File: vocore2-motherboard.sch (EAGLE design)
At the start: 92 parts, among them IC1 AP63205, IC2 FE1.1S, IC3 LM3761MF-3.3, IC4 LM3761MF-3.3, IC5 LM3761MF-3.3, IC6 FT232R, IC7 742G17DBV, J1 RJHSE-5381, J2 TE_1775470-8, J3 AMPHENOL_1140084168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

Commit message: fix: moved LAN_LED_ACT to gpio43
gpio43 can be configured to represent the LNK/ACT state of the Ethernt
PHYs Port 0.
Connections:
- removed net N$47: U1.GPIO43
- new net N$34: U1.GPIO37
- net LED_LAN_ACT: now also IC7B.I, U1.GPIO43; no longer IC7A.I, U1.GPIO37
- net LED_LAN_LNK: now also IC7A.I; no longer IC7B.I
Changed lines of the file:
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@@
 <wire x1="78.74" y1="142.24" x2="78.74" y2="144.78" width="0.1524" layer="91"/>
 <junction x="78.74" y="142.24"/>
+<junction x="40.64" y="142.24"/>
 </segment>
 <segment>
@@
 <net name="LED_LAN_ACT" class="0">
 <segment>
-<pinref part="U1" gate="G$1" pin="GPIO37"/>
-<wire x1="106.68" y1="73.66" x2="109.22" y2="73.66" width="0.1524" layer="91"/>
-<label x="109.22" y="73.66" size="1.27" layer="95" xref="yes"/>
+<pinref part="U1" gate="G$1" pin="GPIO43"/>
+<wire x1="106.68" y1="58.42" x2="111.76" y2="58.42" width="0.1524" layer="91"/>
+<label x="111.76" y="58.42" size="1.27" layer="95" xref="yes"/>
 </segment>
 </net>
@@
 <pinref part="U1" gate="G$1" pin="GPIO42"/>
 <wire x1="106.68" y1="60.96" x2="109.22" y2="60.96" width="0.1524" layer="91"/>
-</segment>
-</net>
-<net name="N$47" class="0">
-<segment>
-<pinref part="U1" gate="G$1" pin="GPIO43"/>
-<wire x1="106.68" y1="58.42" x2="109.22" y2="58.42" width="0.1524" layer="91"/>
 </segment>
 </net>
@@
 <pinref part="SP1" gate="G$1" pin="2"/>
 <wire x1="15.24" y1="25.4" x2="15.24" y2="27.94" width="0.1524" layer="91"/>
+</segment>
+</net>
+<net name="N$34" class="0">
+<segment>
+<pinref part="U1" gate="G$1" pin="GPIO37"/>
+<wire x1="106.68" y1="73.66" x2="109.22" y2="73.66" width="0.1524" layer="91"/>
 </segment>
 </net>
@@
 </segment>
 </net>
-<net name="LED_LAN_ACT" class="0">
+<net name="N$67" class="0">
+<segment>
+<pinref part="IC7" gate="B" pin="O"/>
+<pinref part="R14" gate="G$1" pin="1"/>
+<wire x1="238.76" y1="96.52" x2="215.9" y2="96.52" width="0.1524" layer="91"/>
+</segment>
+</net>
+<net name="LED_LAN_LNK" class="0">
 <segment>
 <pinref part="IC7" gate="A" pin="I"/>
@@
 </segment>
 </net>
-<net name="N$67" class="0">
-<segment>
-<pinref part="IC7" gate="B" pin="O"/>
-<pinref part="R14" gate="G$1" pin="1"/>
-<wire x1="238.76" y1="96.52" x2="215.9" y2="96.52" width="0.1524" layer="91"/>
-</segment>
-</net>
-<net name="LED_LAN_LNK" class="0">
+<net name="VC_3V3" class="0">
+<segment>
+<pinref part="IC7" gate="C" pin="VCC"/>
+<wire x1="233.68" y1="144.78" x2="233.68" y2="147.32" width="0.1524" layer="91"/>
+<label x="233.68" y="147.32" size="1.27" layer="95" rot="R90" xref="yes"/>
+</segment>
+</net>
+<net name="LED_LAN_ACT" class="0">
 <segment>
 <pinref part="IC7" gate="B" pin="I"/>
@@
 </segment>
 </net>
-<net name="VC_3V3" class="0">
-<segment>
-<pinref part="IC7" gate="C" pin="VCC"/>
-<wire x1="233.68" y1="144.78" x2="233.68" y2="147.32" width="0.1524" layer="91"/>
-<label x="233.68" y="147.32" size="1.27" layer="95" rot="R90" xref="yes"/>
-</segment>
-</net>

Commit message: fix: typo in partname LM3761MF -> LM3671MF
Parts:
- IC3, IC4, IC5: value LM3761MF-3.3 -> LM3671MF-3.3
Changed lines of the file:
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@@
 <part name="GND9" library="supply1" deviceset="GND" device=""/>
 <part name="R3" library="rcl" library_urn="urn:adsk.eagle:library:334" deviceset="R-EU_" device="R0603" package3d_urn="urn:adsk.eagle:package:23555/3" value="330R"/>
-<part name="IC4" library="texas" deviceset="LM3671" device="" value="LM3761MF-3.3">
+<part name="IC4" library="texas" deviceset="LM3671" device="" value="LM3671MF-3.3">
 <attribute name="FARNELL" value="1685767"/>
 <attribute name="MBM" value="1"/>
@@
 <part name="GND65" library="supply1" deviceset="GND" device=""/>
 <part name="FRAME4" library="frames" library_urn="urn:adsk.eagle:library:229" deviceset="A4L-LOC" device=""/>
-<part name="IC3" library="texas" deviceset="LM3671" device="" value="LM3761MF-3.3">
+<part name="IC3" library="texas" deviceset="LM3671" device="" value="LM3671MF-3.3">
 <attribute name="FARNELL" value="1685767"/>
 <attribute name="MBM" value="1"/>
@@
 </part>
 <part name="GND14" library="supply1" deviceset="GND" device=""/>
-<part name="IC5" library="texas" deviceset="LM3671" device="" value="LM3761MF-3.3">
+<part name="IC5" library="texas" deviceset="LM3671" device="" value="LM3671MF-3.3">
 <attribute name="FARNELL" value="1685767"/>
 <attribute name="MBM" value="1"/>

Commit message: feat: added digikey part numbers
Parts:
- C11, C13, C32: BUERKLIN 53D2086 -> (none); DIGIKEY (none) -> 1276-2087-1-ND; MBM 10 -> (none); PREIS 0,10 -> (none)
- C20, C21, C22, C23: DIGIKEY (none) -> 490-4780-1-ND
- C24: DIGIKEY (none) -> 399-7246-1-ND
- D4: DIGIKEY (none) -> 1727-3884-1-ND; MBM 5 -> (none); PREIS 0,311 -> (none)
- IC3, IC4, IC5: DIGIKEY (none) -> LM3671MF-3.3/NOPBCT-ND; MBM 1 -> (none); PREIS 0,704 -> (none)
- IC7: DIGIKEY (none) -> 296-SN74LVC2G17DBVRCT-ND; MBM 1 -> (none); PREIS 0,616 -> (none)
- L10, L2, L3: DIGIKEY (none) -> 445-8725-1-ND; MBM 1 -> (none); PREIS 1,70 -> (none)
- L8: DIGIKEY (none) -> 490-1054-1-ND; FARNELL 1515661 -> (none); MBM 10 -> (none); PREIS 0,0595 -> (none)
- Q1: DIGIKEY (none) -> BSS123LT1GOSCT-ND‎
- R1: DIGIKEY (none) -> RR08P2.7KDCT-ND
- R12, R13, R8, R9: value (none) -> 75R; DIGIKEY (none) -> RNCP0603FTD75R0CT-ND‎

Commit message: fix: proper colors for leds
PWR = red
MPCIE_PWR = orange
MPCIE_USB = green
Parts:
- LED1, LED2, LED4: value GREEN -> ORANGE
- LED3: value GREEN -> RED
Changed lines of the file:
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@@
 <attribute name="SPICEPREFIX" value="G"/>
 </part>
-<part name="LED3" library="led" library_urn="urn:adsk.eagle:library:259" deviceset="LED" device="CHIP-LED0805" package3d_urn="urn:adsk.eagle:package:15818/2" value="GREEN">
+<part name="LED3" library="led" library_urn="urn:adsk.eagle:library:259" deviceset="LED" device="CHIP-LED0805" package3d_urn="urn:adsk.eagle:package:15818/2" value="RED">
 <attribute name="FARNELL" value="1686076"/>
 <attribute name="MBM" value="5"/>
@@
 </part>
 <part name="GND17" library="supply1" deviceset="GND" device=""/>
-<part name="LED1" library="led" library_urn="urn:adsk.eagle:library:259" deviceset="LED" device="CHIP-LED0805" package3d_urn="urn:adsk.eagle:package:15818/2" value="GREEN">
+<part name="LED1" library="led" library_urn="urn:adsk.eagle:library:259" deviceset="LED" device="CHIP-LED0805" package3d_urn="urn:adsk.eagle:package:15818/2" value="ORANGE">
 <attribute name="FARNELL" value="1686076"/>
 <attribute name="MBM" value="5"/>
@@
 <part name="GND18" library="supply1" deviceset="GND" device=""/>
 <part name="R2" library="rcl" library_urn="urn:adsk.eagle:library:334" deviceset="R-EU_" device="R0603" package3d_urn="urn:adsk.eagle:package:23555/3" value="330R"/>
-<part name="LED2" library="led" library_urn="urn:adsk.eagle:library:259" deviceset="LED" device="CHIP-LED0805" package3d_urn="urn:adsk.eagle:package:15818/2" value="GREEN">
+<part name="LED2" library="led" library_urn="urn:adsk.eagle:library:259" deviceset="LED" device="CHIP-LED0805" package3d_urn="urn:adsk.eagle:package:15818/2" value="ORANGE">
 <attribute name="FARNELL" value="1686076"/>
 <attribute name="MBM" value="5"/>
@@
 <part name="GND19" library="supply1" deviceset="GND" device=""/>
 <part name="R4" library="rcl" library_urn="urn:adsk.eagle:library:334" deviceset="R-EU_" device="R0603" package3d_urn="urn:adsk.eagle:package:23555/3" value="330R"/>
-<part name="LED4" library="led" library_urn="urn:adsk.eagle:library:259" deviceset="LED" device="CHIP-LED0805" package3d_urn="urn:adsk.eagle:package:15818/2" value="GREEN">
+<part name="LED4" library="led" library_urn="urn:adsk.eagle:library:259" deviceset="LED" device="CHIP-LED0805" package3d_urn="urn:adsk.eagle:package:15818/2" value="ORANGE">
 <attribute name="FARNELL" value="1686076"/>
 <attribute name="MBM" value="5"/>

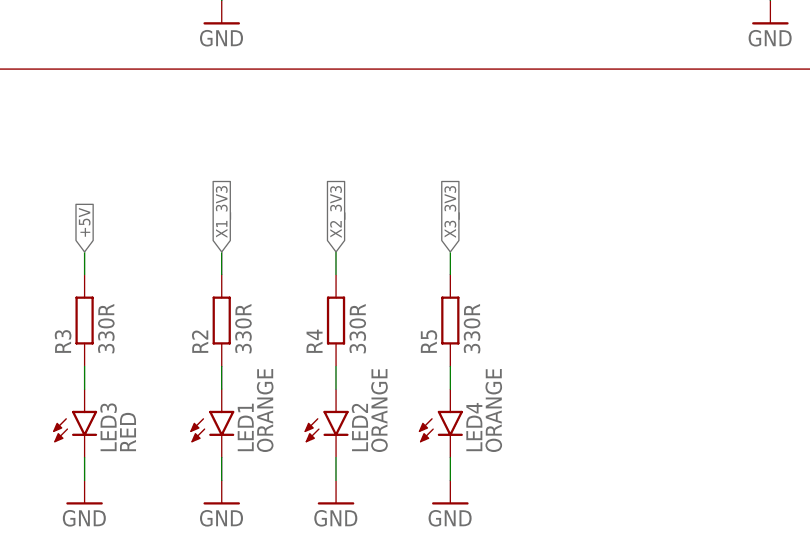
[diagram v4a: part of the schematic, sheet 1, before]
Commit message: fix: corrected led restistor values
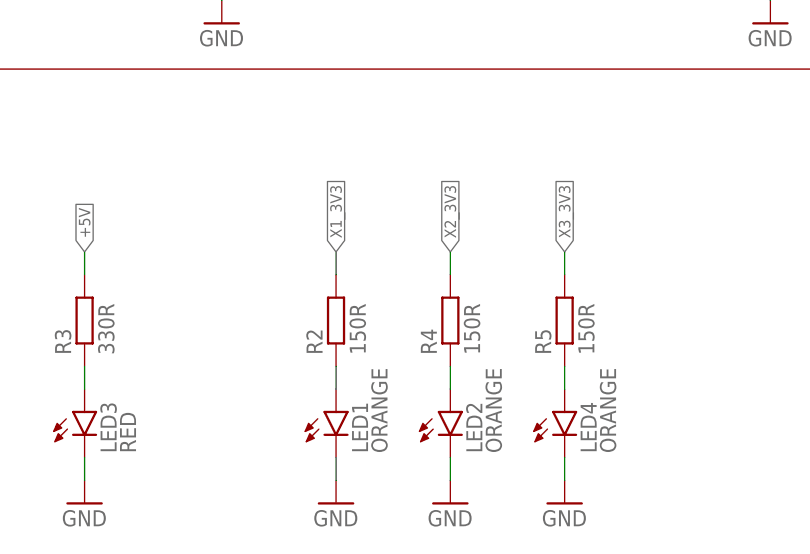
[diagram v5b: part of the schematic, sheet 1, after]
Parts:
- LED1, LED2, LED4: DIGIKEY (none) -> 160-1445-1-ND; FARNELL 1686076 -> (none); MBM 5 -> (none); PREIS 0,20 -> (none); SPICEPREFIX B -> (none)
- LED3: DIGIKEY (none) -> 160-1447-1-ND; FARNELL 1686076 -> (none); MBM 5 -> (none); PREIS 0,20 -> (none); SPICEPREFIX B -> (none)
- LED5, LED6, LED7: DIGIKEY (none) -> 160-1446-1-ND; FARNELL 1686076 -> (none); MBM 5 -> (none); PREIS 0,20 -> (none); SPICEPREFIX B -> (none)
- R10, R2, R4, R5, R6: value 330R -> 150R
- R14, R15: value 330R -> 820R; DIGIKEY (none) -> A129687CT-ND
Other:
- note added: "I=10mA @ Vf=2V"
- moved on the sheet: LED1, LED2, LED4, R2, R4, R5

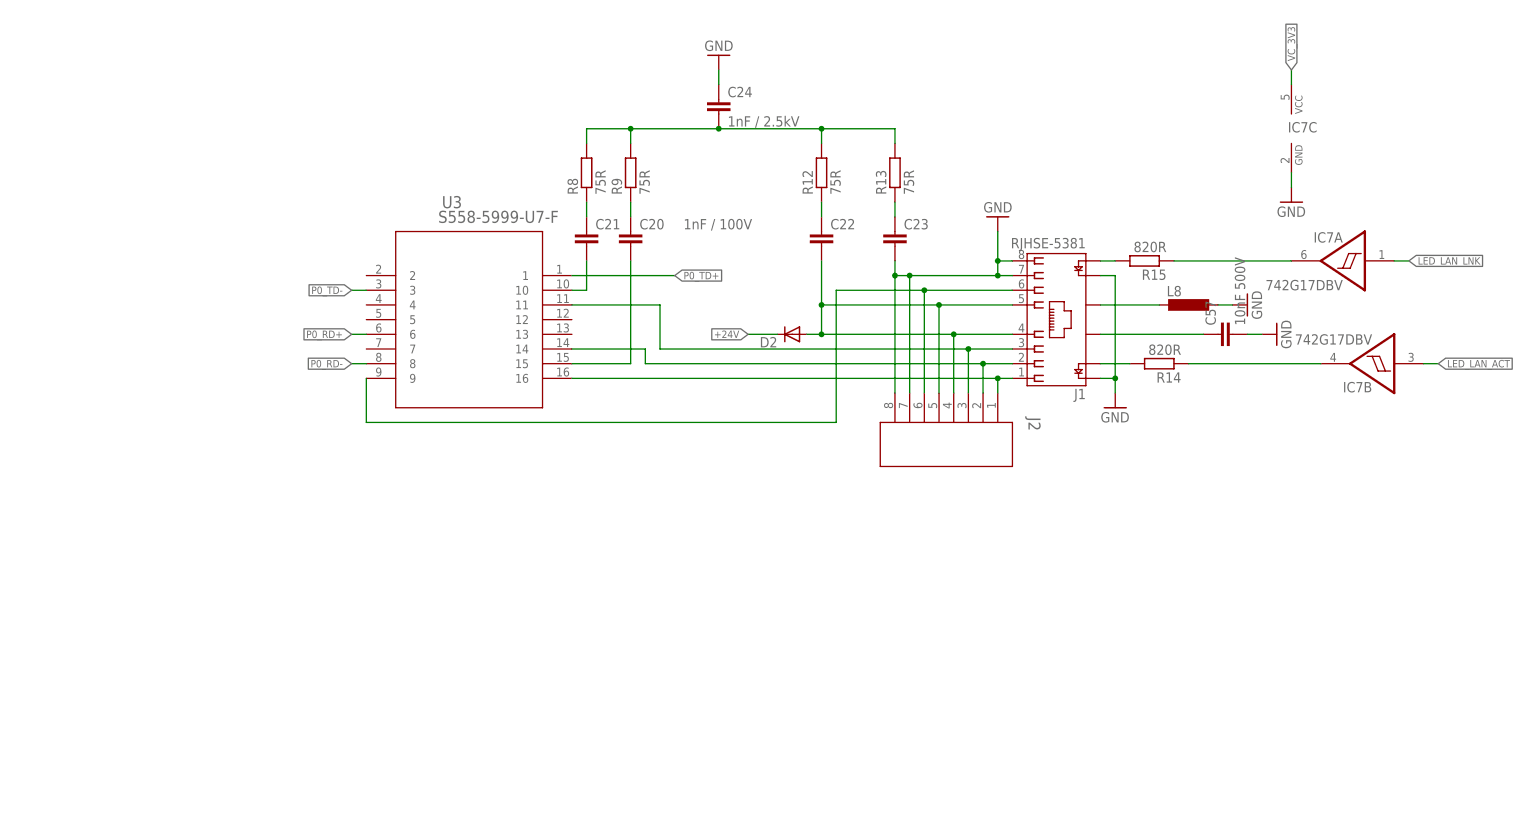
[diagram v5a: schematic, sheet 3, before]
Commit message: fix: some more digikey part numbers
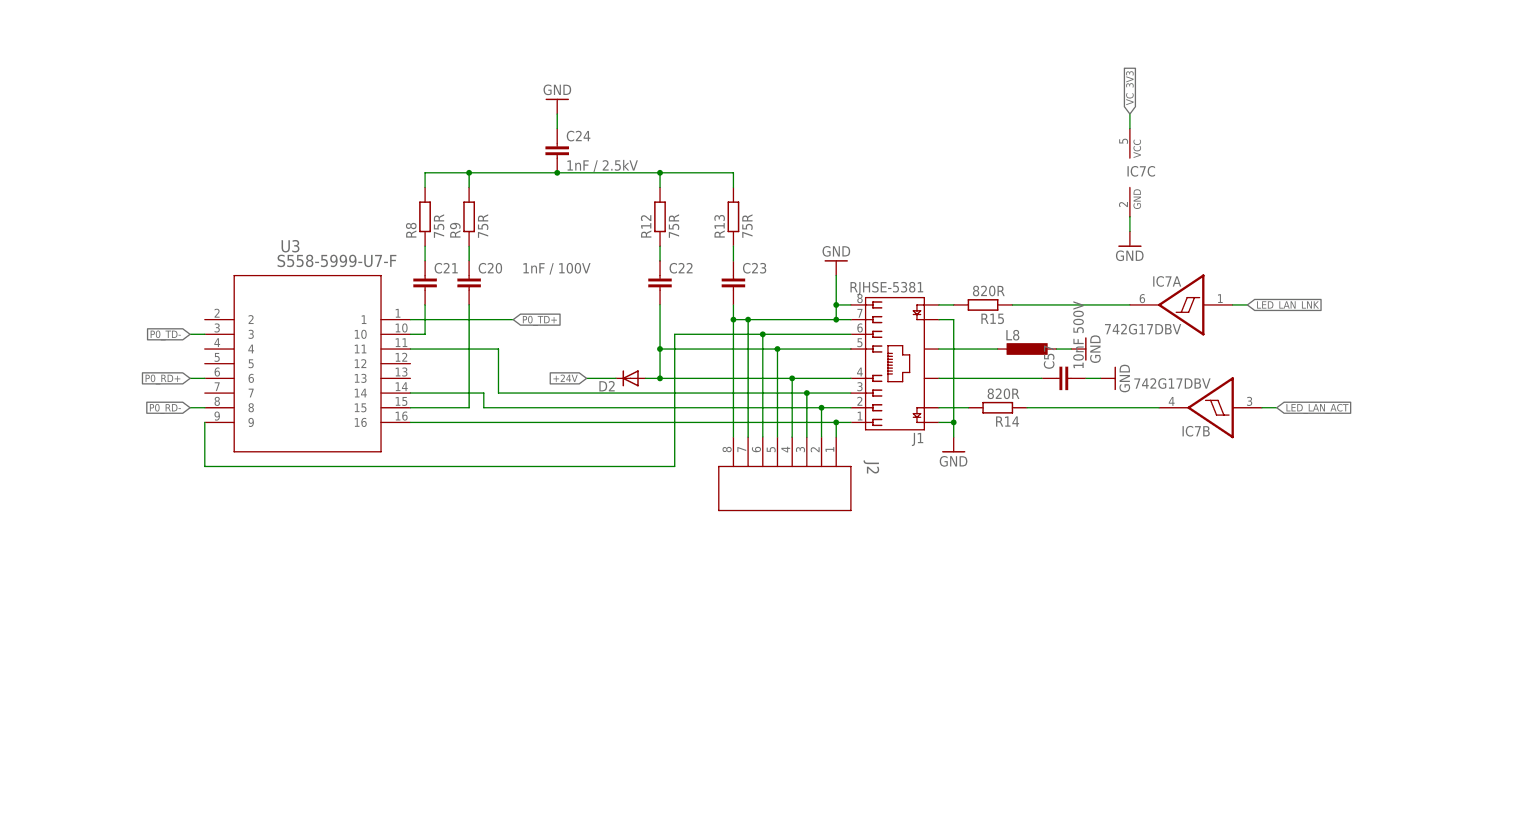
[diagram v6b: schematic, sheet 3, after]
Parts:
- X5: DIGIKEY (none) -> ‎277-1207-ND‎;‎277-13872-ND‎
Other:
- moved on the sheet: C20, C21, C22, C23, C24, C57, D2, IC7A, IC7B, IC7C, J1, J2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

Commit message: refactor: new symbol for ethernet transformer U4
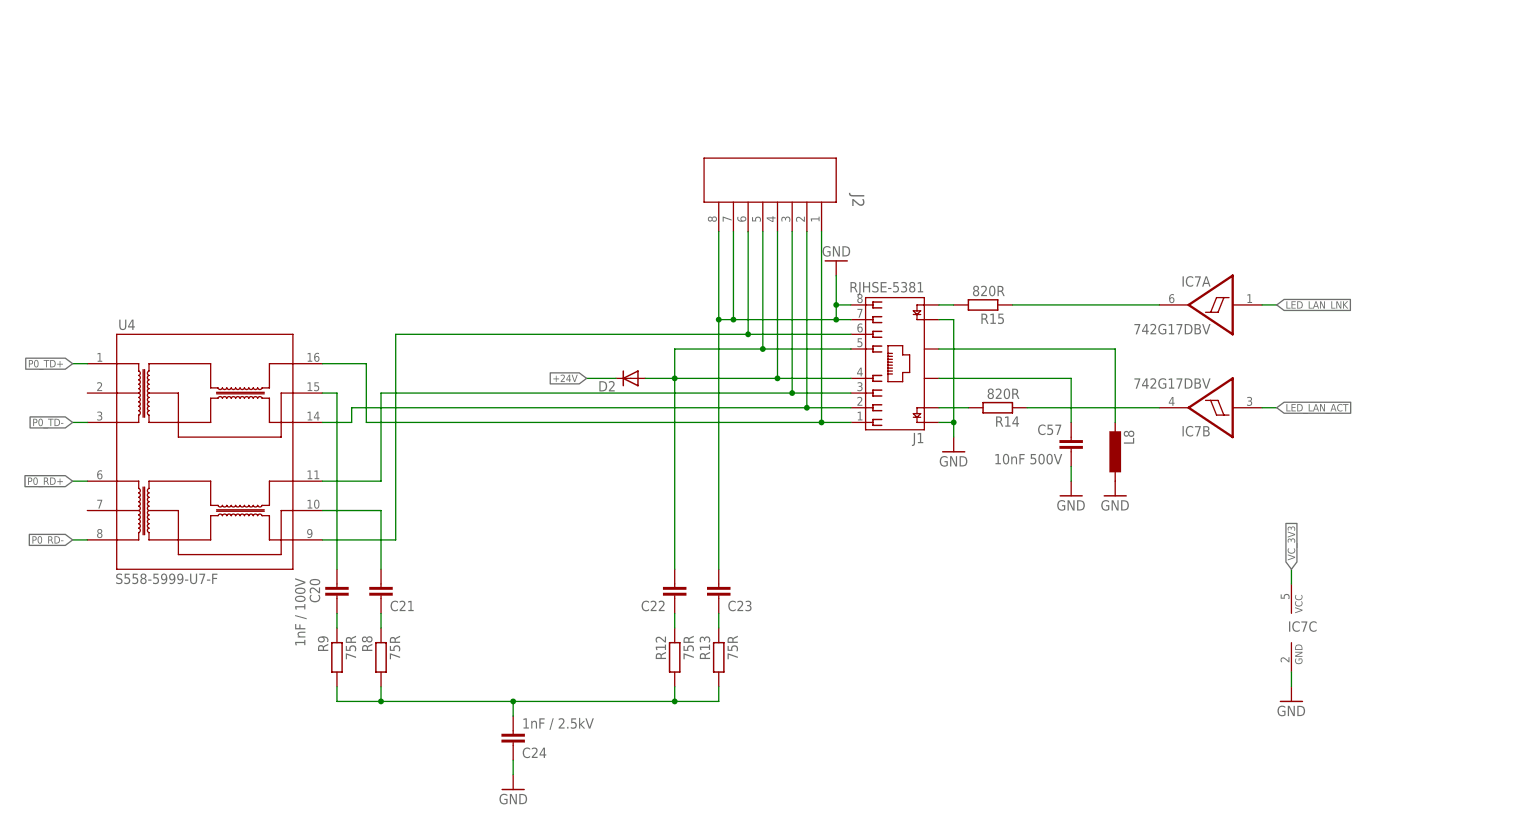
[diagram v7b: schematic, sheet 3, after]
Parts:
- removed U3: S558-5999-U7-F, ethernet-transformer:S558-5999-U7-F
- added U4: S558-5999-U7-F, ethernet-transformer:S558-5999-U7-F
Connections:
- net N$16: now also U4.RX_CT; no longer U3.10
- net N$7: now also U4.TX_CT; no longer U3.15
- net P0_RD+: now also U4.RD+; no longer U3.6
- net P0_RD-: now also U4.RD-; no longer U3.8
- net P0_TD+: now also U4.TD+; no longer U3.1
- net P0_TD-: now also U4.TD-; no longer U3.3
- net RX+: now also U4.RX+; no longer U3.11
- net RX-: now also U4.RX-; no longer U3.9
- net TX+: now also U4.TX+; no longer U3.16
- net TX-: now also U4.TX-; no longer U3.14
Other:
- moved on the sheet: C20, C21, C22, C23, C24, C57, IC7A, IC7C, J2, L8, R12, R13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

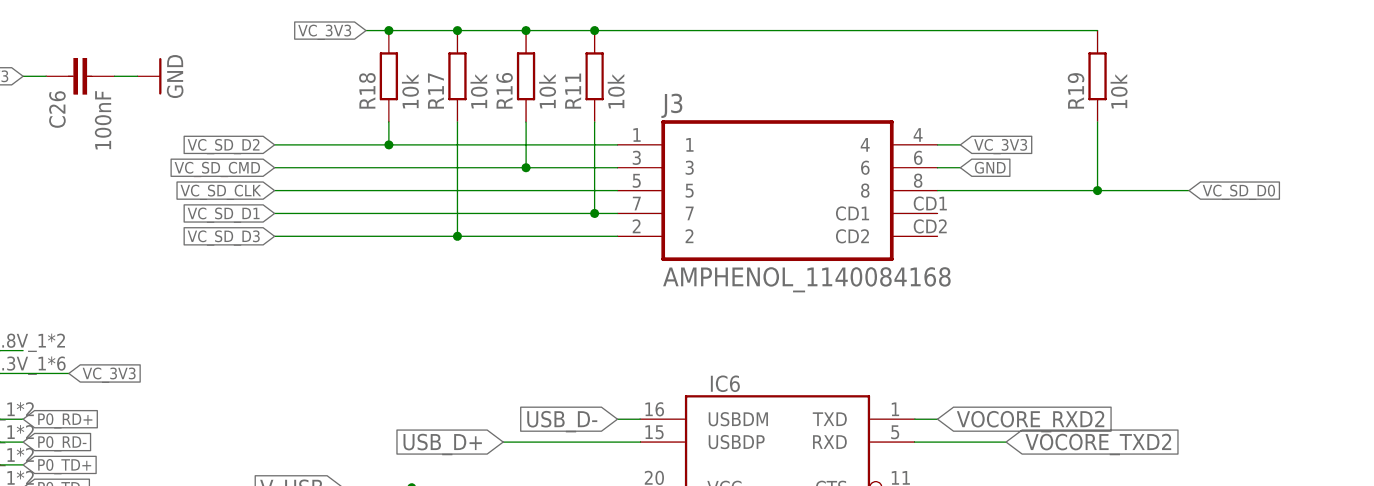
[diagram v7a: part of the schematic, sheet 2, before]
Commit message: fix: switched SD_D0 and SD_D1
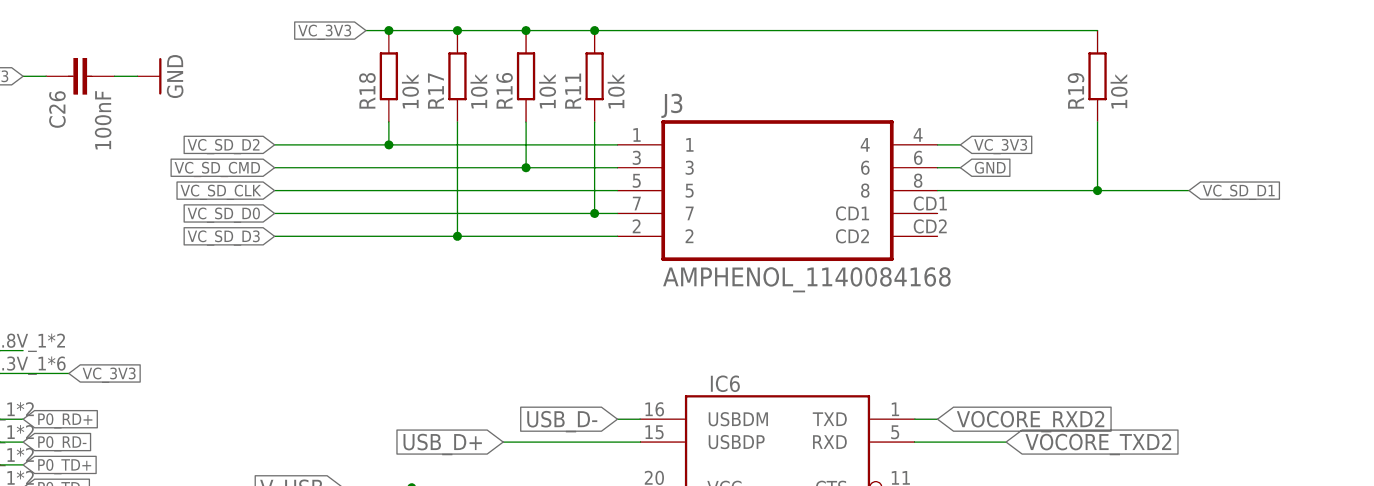
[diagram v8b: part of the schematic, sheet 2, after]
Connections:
- net VC_SD_D0: now also J3.7, R11.1; no longer J3.8, R19.1
- net VC_SD_D1: now also J3.8, R19.1; no longer J3.7, R11.1
